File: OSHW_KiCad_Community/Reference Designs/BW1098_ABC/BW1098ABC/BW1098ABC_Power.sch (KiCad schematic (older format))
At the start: 32 parts

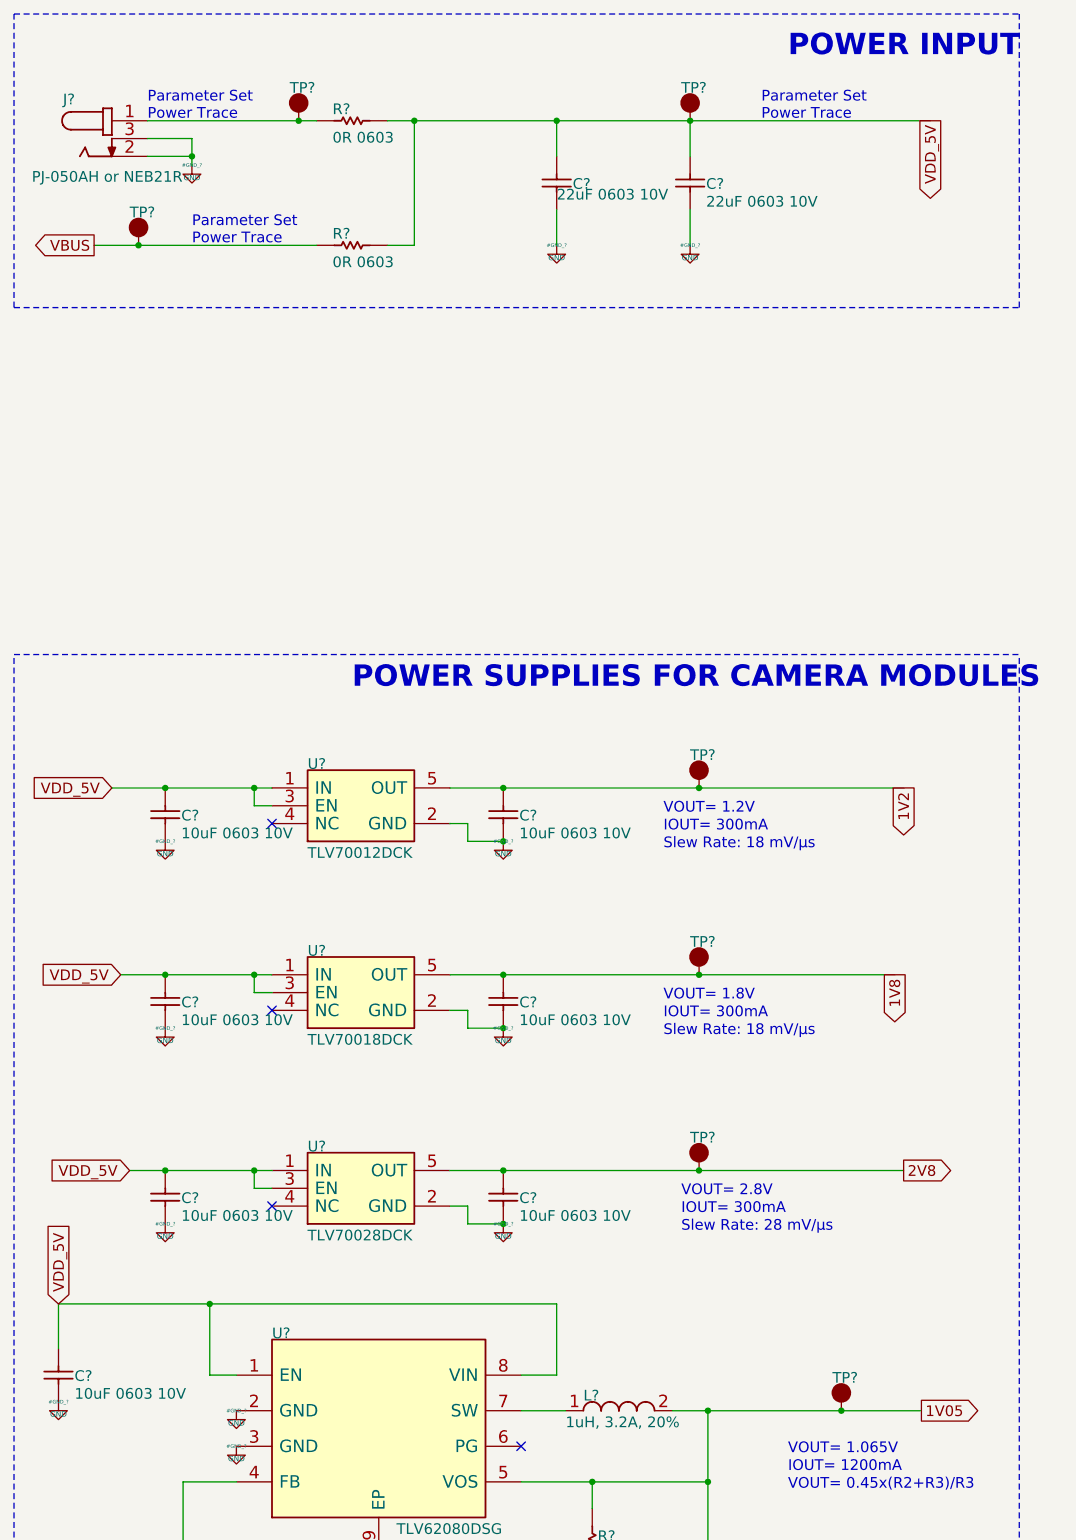
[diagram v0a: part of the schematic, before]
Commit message: schematic edits for BW1098ABC
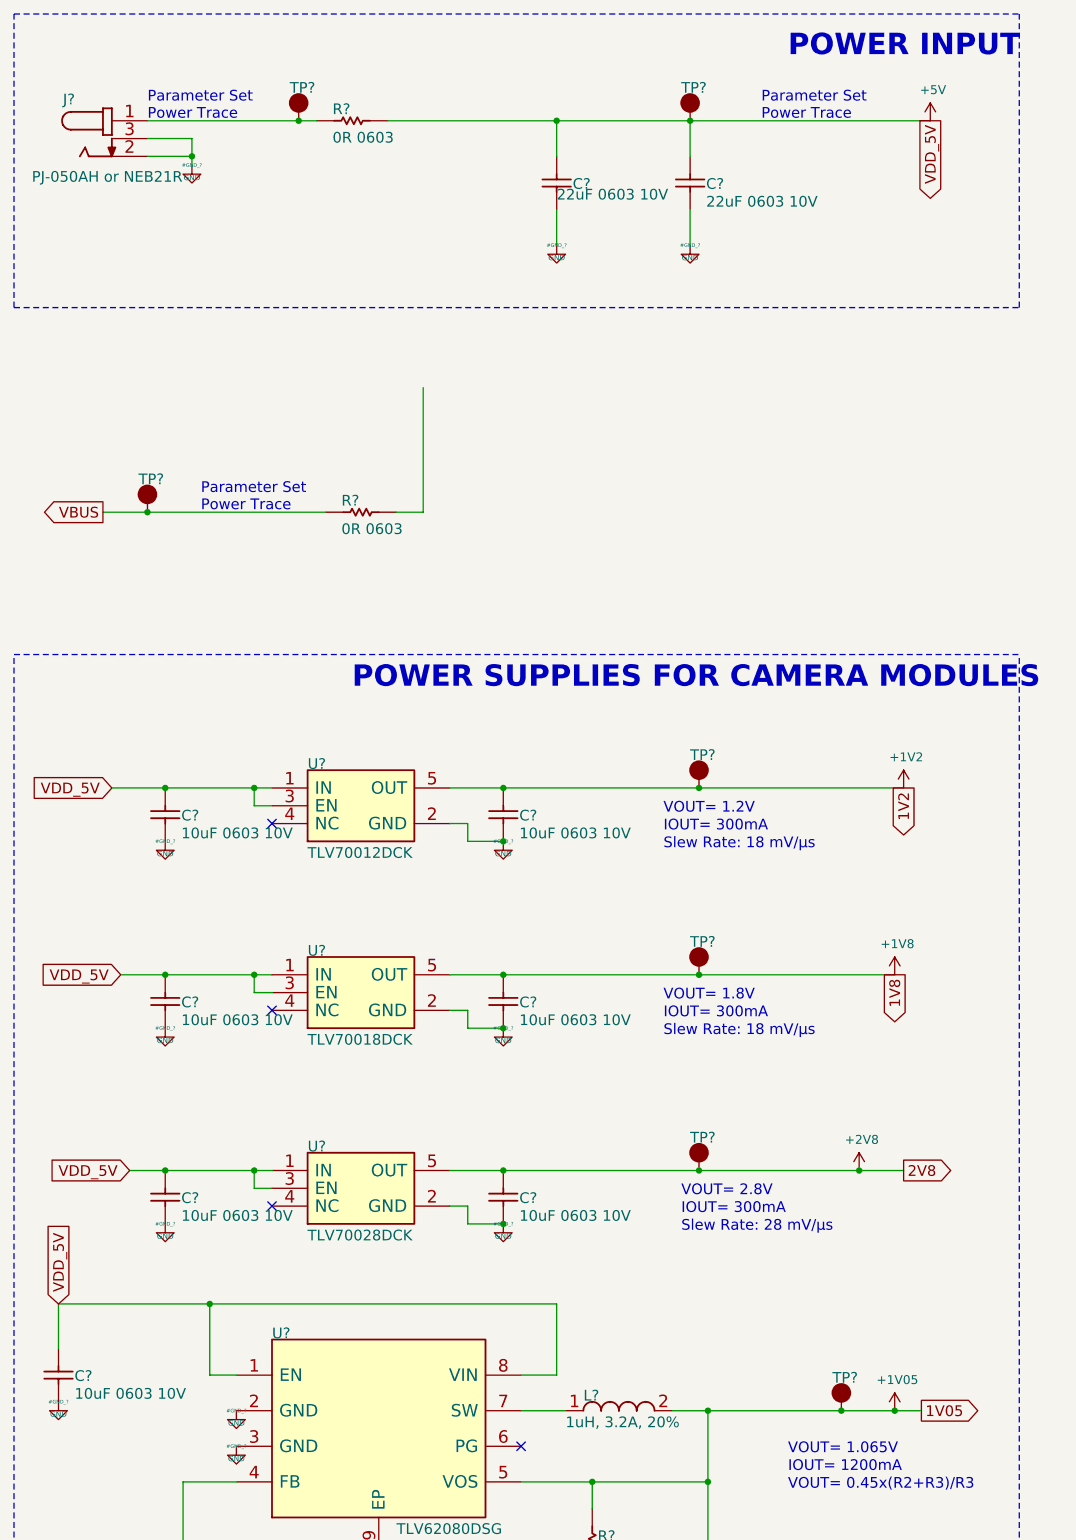
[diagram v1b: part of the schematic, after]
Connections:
- net 1V05 renamed +1V0
- net 1V2 renamed +1V2
- net 1V8 renamed +1V8
- net 2V8 renamed +2V8
- net VDD_5V renamed +5V
- net +5V: no longer R?.2
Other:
- moved on the sheet: R?, TP?
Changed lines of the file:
@@
 	2050 8150 1200 8150
 Wire Wire Line
-	3200 2200 3200 1500
-Wire Wire Line
-	3050 2200 3200 2200
+	3250 3700 3250 3000
+Wire Wire Line
+	3100 3700 3250 3700
 Wire Wire Line
 	1950 1700 1700 1700
@@
 Wire Wire Line
 	4000 1500 4750 1500
-Wire Wire Line
-	3200 1500 4000 1500
-Wire Wire Line
-	3050 1500 3200 1500
 Wire Wire Line
 	3500 5450 3400 5450
@@
 Connection ~ 2300 6300
 Connection ~ 2300 5250
-Connection ~ 3200 1500
 Connection ~ 4000 1500
 Connection ~ 4200 9800
@@
 L depthAI_sch:TEST_POINT TP?
 U 1 1 604BD5AB
-P 1650 2200
+P 1700 3700
 AR Path="/5FD7EFCB/604BD5AB" Ref="TP?"  Part="1"
 AR Path="/604AEAFA/604BD5AB" Ref="TP?"  Part="1"
-F 0 "TP?" H 1600 2350 60  0000 L BNN
-F 1 "TEST_POINT" H 1650 2200 50  0001 C CNN
-F 2 "TestPoint:TestPoint_Loop_D1.80mm_Drill1.0mm_Beaded" H 1650 2200 50  0001 C CNN
-F 3 "" H 1650 2200 50  0001 C CNN
-	1    1650 2200
+F 0 "TP?" H 1650 3850 60  0000 L BNN
+F 1 "TEST_POINT" H 1700 3700 50  0001 C CNN
+F 2 "TestPoint:TestPoint_Loop_D1.80mm_Drill1.0mm_Beaded" H 1700 3700 50  0001 C CNN
+F 3 "" H 1700 3700 50  0001 C CNN
+	1    1700 3700
 	1    0    0    -1
 $EndComp
@@
 L depthAI_sch:CRCW06030000Z0EA R?
 U 1 1 604BD5C9
-P 2650 2200
+P 2700 3700
 AR Path="/5FD7EFCB/604BD5C9" Ref="R?"  Part="1"
 AR Path="/604AEAFA/604BD5C9" Ref="R?"  Part="1"
-F 0 "R?" H 2740 2230 60  0000 L BNN
-F 1 "0R 0603" H 2740 2070 60  0000 L BNN
-F 2 "Resistor_SMD:R_0402_1005Metric" H 2740 2070 60  0001 C CNN
-F 3 "" H 2740 2070 60  0000 C CNN
-	1    2650 2200
+F 0 "R?" H 2790 3730 60  0000 L BNN
+F 1 "0R 0603" H 2790 3570 60  0000 L BNN
+F 2 "Resistor_SMD:R_0402_1005Metric" H 2790 3570 60  0001 C CNN
+F 3 "" H 2790 3570 60  0000 C CNN
+	1    2700 3700
 	1    0    0    -1
 $EndComp
@@
 	1600 7400 1800 7400
 Wire Wire Line
-	1400 2200 1650 2200
+	1450 3700 1700 3700
 Wire Wire Line
 	1550 6300 1800 6300
@@
 Text GLabel 6050 8750 2    60   Output ~ 0
 1V05
-Text GLabel 1400 2200 0    60   Output ~ 0
+Text GLabel 1450 3700 0    60   Output ~ 0
 VBUS
 Text GLabel 6100 1500 3    60   Output ~ 0
@@
 Text Notes 5150 1500 0    60   ~ 0
 Parameter Set\nPower Trace
-Text Notes 1950 2200 0    60   ~ 0
+Text Notes 2000 3700 0    60   ~ 0
 Parameter Set\nPower Trace
 Text GLabel 5950 5250 3    60   Output ~ 0
@@
 Text GLabel 1500 5250 0    60   Input ~ 0
 VDD_5V
-Connection ~ 1650 2200
-Wire Wire Line
-	1650 2200 2650 2200
+Connection ~ 1700 3700
+Wire Wire Line
+	1700 3700 2700 3700
 Connection ~ 1800 5250
 Wire Wire Line
@@
 Connection ~ 4800 7400
 Wire Wire Line
-	4800 7400 5950 7400
+	4800 7400 5700 7400
 Connection ~ 5600 8750
 Wire Wire Line
-	5600 8750 6050 8750
+	5600 8750 5900 8750
+$Comp
+L power:+5V #PWR?
+U 1 1 5FFB0F72
+P 6100 1500
+F 0 "#PWR?" H 6100 1350 50  0001 C CNN
+F 1 "+5V" H 6115 1673 50  0000 C CNN
+F 2 "" H 6100 1500 50  0001 C CNN
+F 3 "" H 6100 1500 50  0001 C CNN
+	1    6100 1500
+	1    0    0    -1
+$EndComp
+$Comp
+L power:+1V2 #PWR?
+U 1 1 5FFB5C52
+P 5950 5250
+F 0 "#PWR?" H 5950 5100 50  0001 C CNN
+F 1 "+1V2" H 5965 5423 50  0000 C CNN
+F 2 "" H 5950 5250 50  0001 C CNN
+F 3 "" H 5950 5250 50  0001 C CNN
+	1    5950 5250
+	1    0    0    -1
+$EndComp
+$Comp
+L power:+1V8 #PWR?
+U 1 1 5FFB659A
+P 5900 6300
+F 0 "#PWR?" H 5900 6150 50  0001 C CNN
+F 1 "+1V8" H 5915 6473 50  0000 C CNN
+F 2 "" H 5900 6300 50  0001 C CNN
+F 3 "" H 5900 6300 50  0001 C CNN
+	1    5900 6300
+	1    0    0    -1
+$EndComp
+$Comp
+L power:+2V8 #PWR?
+U 1 1 5FFB6C28
+P 5700 7400
+F 0 "#PWR?" H 5700 7250 50  0001 C CNN
+F 1 "+2V8" H 5715 7573 50  0000 C CNN
+F 2 "" H 5700 7400 50  0001 C CNN
+F 3 "" H 5700 7400 50  0001 C CNN
+	1    5700 7400
+	1    0    0    -1
+$EndComp
+Connection ~ 5700 7400
+Wire Wire Line
+	5700 7400 5950 7400
+$Comp
+L depthAI_sch:+1V05 #PWR?
+U 1 1 5FFBECAB
+P 5900 8750
+F 0 "#PWR?" H 5900 8600 50  0001 C CNN
+F 1 "+1V05" H 5915 8923 50  0000 C CNN
+F 2 "" H 5900 8750 50  0001 C CNN
+F 3 "" H 5900 8750 50  0001 C CNN
+	1    5900 8750
+	1    0    0    -1
+$EndComp
+Connection ~ 5900 8750
+Wire Wire Line
+	5900 8750 6050 8750
+Wire Wire Line
+	3050 1500 4000 1500
 $EndSCHEMATC

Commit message: small stuff
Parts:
- C? (x3): value 22uF 0603 10V -> 22uF 0603; symbol depthAI_sch:GRM155R60J106ME15D -> BW1098ABC-rescue:GRM155R60J106ME15D-depthAI_sch
- C? (x7): value 10uF 0603 10V -> 10uF 0603; symbol depthAI_sch:GRM188R61A106ME69D -> BW1098ABC-rescue:GRM188R61A106ME69D-depthAI_sch
- J?: symbol depthAI_sch:PJ-050AH_NEB21R_COMBO -> BW1098ABC-rescue:PJ-050AH_NEB21R_COMBO-depthAI_sch
- J?: symbol depthAI_sch:B2B-PH-K-S(LF)(SN) -> BW1098ABC-rescue:B2B-PH-K-S(LF)(SN)-depthAI_sch
- L?: symbol depthAI_sch:DFE252012P-1R0M -> BW1098ABC-rescue:DFE252012P-1R0M-depthAI_sch
- R?: symbol depthAI_sch:CRCW040253K6FKED -> BW1098ABC-rescue:CRCW040253K6FKED-depthAI_sch
- R?: symbol depthAI_sch:CRCW040239K2FKED -> BW1098ABC-rescue:CRCW040239K2FKED-depthAI_sch
- R? (x2): symbol depthAI_sch:CRCW06030000Z0EA -> BW1098ABC-rescue:CRCW06030000Z0EA-depthAI_sch
- TP? (x11): symbol depthAI_sch:TEST_POINT -> BW1098ABC-rescue:TEST_POINT-depthAI_sch
- U?: symbol depthAI_sch:TLV70012DCK -> BW1098ABC-rescue:TLV70012DCK-depthAI_sch
- U?: symbol depthAI_sch:TLV70028DCK -> BW1098ABC-rescue:TLV70028DCK-depthAI_sch
- U?: symbol depthAI_sch:TLV70018DCK -> BW1098ABC-rescue:TLV70018DCK-depthAI_sch
- U?: symbol depthAI_sch:TLV62080DSG -> BW1098ABC-rescue:TLV62080DSG-depthAI_sch
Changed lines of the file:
@@
 Connection ~ 4850 8750
 $Comp
-L depthAI_sch:PJ-050AH_NEB21R_COMBO J?
+L BW1098ABC-rescue:PJ-050AH_NEB21R_COMBO-depthAI_sch J?
 U 1 1 604BD4F2
 P 1700 1500
@@
 $EndComp
 $Comp
-L depthAI_sch:GRM155R60J106ME15D C?
+L BW1098ABC-rescue:GRM155R60J106ME15D-depthAI_sch C?
 U 1 1 604BD4F9
 P 4750 2000
@@
 AR Path="/604AEAFA/604BD4F9" Ref="C?"  Part="1"
 F 0 "C?" V 4860 1910 60  0000 R TNN
-F 1 "22uF 0603 10V" V 4760 1910 60  0000 R TNN
+F 1 "22uF 0603" V 4760 1910 60  0000 R TNN
 F 2 "Capacitor_SMD:C_0201_0603Metric" H 4760 1910 60  0001 C CNN
 F 3 "" H 4760 1910 60  0000 C CNN
@@
 $EndComp
 $Comp
-L depthAI_sch:GRM155R60J106ME15D C?
+L BW1098ABC-rescue:GRM155R60J106ME15D-depthAI_sch C?
 U 1 1 604BD507
 P 4850 9950
@@
 AR Path="/604AEAFA/604BD507" Ref="C?"  Part="1"
 F 0 "C?" V 4960 9860 60  0000 R TNN
-F 1 "22uF 0603 10V" V 4860 9860 60  0000 R TNN
+F 1 "22uF 0603" V 4860 9860 60  0000 R TNN
 F 2 "Capacitor_SMD:C_0201_0603Metric" H 4860 9860 60  0001 C CNN
 F 3 "" H 4860 9860 60  0000 C CNN
@@
 $EndComp
 $Comp
-L depthAI_sch:GRM188R61A106ME69D C?
+L BW1098ABC-rescue:GRM188R61A106ME69D-depthAI_sch C?
 U 1 1 604BD50E
 P 1800 6600
@@
 AR Path="/604AEAFA/604BD50E" Ref="C?"  Part="1"
 F 0 "C?" V 1910 6510 60  0000 R TNN
-F 1 "10uF 0603 10V" V 1810 6510 60  0000 R TNN
+F 1 "10uF 0603" V 1810 6510 60  0000 R TNN
 F 2 "Capacitor_SMD:C_0201_0603Metric" H 1810 6510 60  0001 C CNN
 F 3 "" H 1810 6510 60  0000 C CNN
@@
 $EndComp
 $Comp
-L depthAI_sch:GRM188R61A106ME69D C?
+L BW1098ABC-rescue:GRM188R61A106ME69D-depthAI_sch C?
 U 1 1 604BD515
 P 1800 7700
@@
 AR Path="/604AEAFA/604BD515" Ref="C?"  Part="1"
 F 0 "C?" V 1910 7610 60  0000 R TNN
-F 1 "10uF 0603 10V" V 1810 7610 60  0000 R TNN
+F 1 "10uF 0603" V 1810 7610 60  0000 R TNN
 F 2 "Capacitor_SMD:C_0201_0603Metric" H 1810 7610 60  0001 C CNN
 F 3 "" H 1810 7610 60  0000 C CNN
@@
 $EndComp
 $Comp
-L depthAI_sch:GRM188R61A106ME69D C?
+L BW1098ABC-rescue:GRM188R61A106ME69D-depthAI_sch C?
 U 1 1 604BD51C
 P 1200 8700
@@
 AR Path="/604AEAFA/604BD51C" Ref="C?"  Part="1"
 F 0 "C?" V 1310 8610 60  0000 R TNN
-F 1 "10uF 0603 10V" V 1210 8610 60  0000 R TNN
+F 1 "10uF 0603" V 1210 8610 60  0000 R TNN
 F 2 "Capacitor_SMD:C_0201_0603Metric" H 1210 8610 60  0001 C CNN
 F 3 "" H 1210 8610 60  0000 C CNN
@@
 $EndComp
 $Comp
-L depthAI_sch:CRCW040253K6FKED R?
+L BW1098ABC-rescue:CRCW040253K6FKED-depthAI_sch R?
 U 1 1 604BD522
 P 4200 9700
@@
 $EndComp
 $Comp
-L depthAI_sch:CRCW040239K2FKED R?
+L BW1098ABC-rescue:CRCW040239K2FKED-depthAI_sch R?
 U 1 1 604BD528
 P 4200 10300
@@
 $EndComp
 $Comp
-L depthAI_sch:GRM188R61A106ME69D C?
+L BW1098ABC-rescue:GRM188R61A106ME69D-depthAI_sch C?
 U 1 1 604BD536
 P 3700 6600
@@
 AR Path="/604AEAFA/604BD536" Ref="C?"  Part="1"
 F 0 "C?" V 3810 6510 60  0000 R TNN
-F 1 "10uF 0603 10V" V 3710 6510 60  0000 R TNN
+F 1 "10uF 0603" V 3710 6510 60  0000 R TNN
 F 2 "Capacitor_SMD:C_0201_0603Metric" H 3710 6510 60  0001 C CNN
 F 3 "" H 3710 6510 60  0000 C CNN
@@
 $EndComp
 $Comp
-L depthAI_sch:GRM188R61A106ME69D C?
+L BW1098ABC-rescue:GRM188R61A106ME69D-depthAI_sch C?
 U 1 1 604BD543
 P 3700 7700
@@
 AR Path="/604AEAFA/604BD543" Ref="C?"  Part="1"
 F 0 "C?" V 3810 7610 60  0000 R TNN
-F 1 "10uF 0603 10V" V 3710 7610 60  0000 R TNN
+F 1 "10uF 0603" V 3710 7610 60  0000 R TNN
 F 2 "Capacitor_SMD:C_0201_0603Metric" H 3710 7610 60  0001 C CNN
 F 3 "" H 3710 7610 60  0000 C CNN
@@
 $EndComp
 $Comp
-L depthAI_sch:DFE252012P-1R0M L?
+L BW1098ABC-rescue:DFE252012P-1R0M-depthAI_sch L?
 U 1 1 604BD549
 P 4050 8750
@@
 $EndComp
 $Comp
-L depthAI_sch:GRM188R61A106ME69D C?
+L BW1098ABC-rescue:GRM188R61A106ME69D-depthAI_sch C?
 U 1 1 604BD550
 P 3700 5550
@@
 AR Path="/604AEAFA/604BD550" Ref="C?"  Part="1"
 F 0 "C?" V 3810 5460 60  0000 R TNN
-F 1 "10uF 0603 10V" V 3710 5460 60  0000 R TNN
+F 1 "10uF 0603" V 3710 5460 60  0000 R TNN
 F 2 "Capacitor_SMD:C_0201_0603Metric" H 3710 5460 60  0001 C CNN
 F 3 "" H 3710 5460 60  0000 C CNN
@@
 $EndComp
 $Comp
-L depthAI_sch:GRM188R61A106ME69D C?
+L BW1098ABC-rescue:GRM188R61A106ME69D-depthAI_sch C?
 U 1 1 604BD557
 P 1800 5550
@@
 AR Path="/604AEAFA/604BD557" Ref="C?"  Part="1"
 F 0 "C?" V 1910 5460 60  0000 R TNN
-F 1 "10uF 0603 10V" V 1810 5460 60  0000 R TNN
+F 1 "10uF 0603" V 1810 5460 60  0000 R TNN
 F 2 "Capacitor_SMD:C_0201_0603Metric" H 1810 5460 60  0001 C CNN
 F 3 "" H 1810 5460 60  0000 C CNN
@@
 $EndComp
 $Comp
-L depthAI_sch:TLV70012DCK U?
+L BW1098ABC-rescue:TLV70012DCK-depthAI_sch U?
 U 1 1 604BD55D
 P 2400 5250
@@
 $EndComp
 $Comp
-L depthAI_sch:TEST_POINT TP?
+L BW1098ABC-rescue:TEST_POINT-depthAI_sch TP?
 U 1 1 604BD563
 P 2550 1500
@@
 $EndComp
 $Comp
-L depthAI_sch:TEST_POINT TP?
+L BW1098ABC-rescue:TEST_POINT-depthAI_sch TP?
 U 1 1 604BD569
 P 4750 1500
@@
 $EndComp
 $Comp
-L depthAI_sch:TEST_POINT TP?
+L BW1098ABC-rescue:TEST_POINT-depthAI_sch TP?
 U 1 1 604BD575
 P 4800 5250
@@
 $EndComp
 $Comp
-L depthAI_sch:TEST_POINT TP?
+L BW1098ABC-rescue:TEST_POINT-depthAI_sch TP?
 U 1 1 604BD57B
 P 4800 6300
@@
 $EndComp
 $Comp
-L depthAI_sch:TLV70028DCK U?
+L BW1098ABC-rescue:TLV70028DCK-depthAI_sch U?
 U 1 1 604BD581
 P 2400 7400
@@
 $EndComp
 $Comp
-L depthAI_sch:TEST_POINT TP?
+L BW1098ABC-rescue:TEST_POINT-depthAI_sch TP?
 U 1 1 604BD587
 P 4800 7400
@@
 $EndComp
 $Comp
-L depthAI_sch:TEST_POINT TP?
+L BW1098ABC-rescue:TEST_POINT-depthAI_sch TP?
 U 1 1 604BD58D
 P 5600 8750
@@
 $EndComp
 $Comp
-L depthAI_sch:TEST_POINT TP?
+L BW1098ABC-rescue:TEST_POINT-depthAI_sch TP?
 U 1 1 604BD593
 P 9750 10050
@@
 $EndComp
 $Comp
-L depthAI_sch:TEST_POINT TP?
+L BW1098ABC-rescue:TEST_POINT-depthAI_sch TP?
 U 1 1 604BD599
 P 10050 10050
@@
 $EndComp
 $Comp
-L depthAI_sch:TEST_POINT TP?
+L BW1098ABC-rescue:TEST_POINT-depthAI_sch TP?
 U 1 1 604BD59F
 P 10400 10050
@@
 $EndComp
 $Comp
-L depthAI_sch:TEST_POINT TP?
+L BW1098ABC-rescue:TEST_POINT-depthAI_sch TP?
 U 1 1 604BD5A5
 P 10750 10050
@@
 $EndComp
 $Comp
-L depthAI_sch:TEST_POINT TP?
+L BW1098ABC-rescue:TEST_POINT-depthAI_sch TP?
 U 1 1 604BD5AB
 P 1700 3700
@@
 $EndComp
 $Comp
-L depthAI_sch:TLV70018DCK U?
+L BW1098ABC-rescue:TLV70018DCK-depthAI_sch U?
 U 1 1 604BD5B1
 P 2400 6300
@@
 $EndComp
 $Comp
-L depthAI_sch:TLV62080DSG U?
+L BW1098ABC-rescue:TLV62080DSG-depthAI_sch U?
 U 1 1 604BD5B7
 P 2200 8550
@@
 $EndComp
 $Comp
-L depthAI_sch:B2B-PH-K-S(LF)(SN) J?
+L BW1098ABC-rescue:B2B-PH-K-S(LF)(SN)-depthAI_sch J?
 U 1 1 604BD5BD
 P 14100 7750
@@
 $EndComp
 $Comp
-L depthAI_sch:CRCW06030000Z0EA R?
+L BW1098ABC-rescue:CRCW06030000Z0EA-depthAI_sch R?
 U 1 1 604BD5C3
 P 2650 1500
@@
 $EndComp
 $Comp
-L depthAI_sch:CRCW06030000Z0EA R?
+L BW1098ABC-rescue:CRCW06030000Z0EA-depthAI_sch R?
 U 1 1 604BD5C9
 P 2700 3700
@@
 $EndComp
 $Comp
-L depthAI_sch:GRM155R60J106ME15D C?
+L BW1098ABC-rescue:GRM155R60J106ME15D-depthAI_sch C?
 U 1 1 604BD5D0
 P 4000 2000
@@
 AR Path="/604AEAFA/604BD5D0" Ref="C?"  Part="1"
 F 0 "C?" V 4110 1910 60  0000 R TNN
-F 1 "22uF 0603 10V" V 4050 2000 60  0000 R TNN
+F 1 "22uF 0603" V 4050 2000 60  0000 R TNN
 F 2 "Capacitor_SMD:C_0201_0603Metric" H 4010 1910 60  0001 C CNN
 F 3 "" H 4010 1910 60  0000 C CNN
@@
 	5700 7400 5950 7400
 $Comp
-L depthAI_sch:+1V05 #PWR?
+L BW1098ABC-rescue:+1V05-depthAI_sch #PWR?
 U 1 1 5FFBECAB
 P 5900 8750
